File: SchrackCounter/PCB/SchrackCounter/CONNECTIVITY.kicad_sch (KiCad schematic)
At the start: 19 parts, among them J2 TYPE-C-31-M-12 (USB C CONN), U6 USBLC6-2SC6

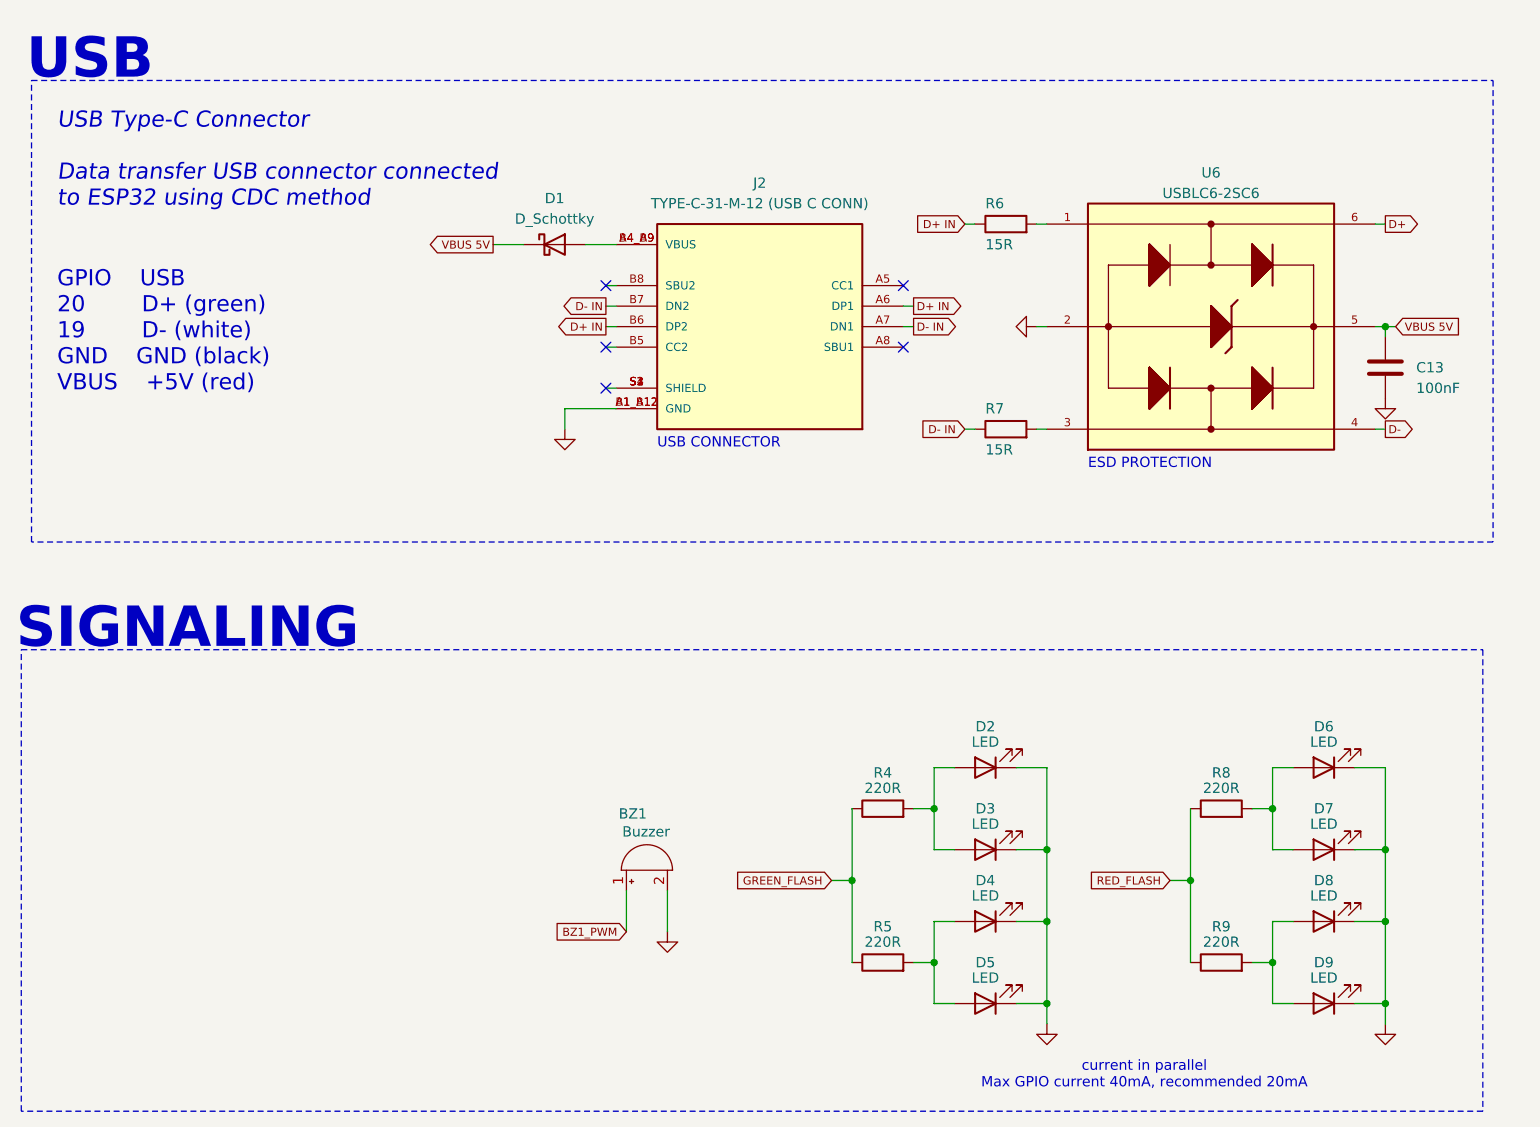
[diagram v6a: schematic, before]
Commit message: Schematic and PCB update
LDO Regulator, and some layout update
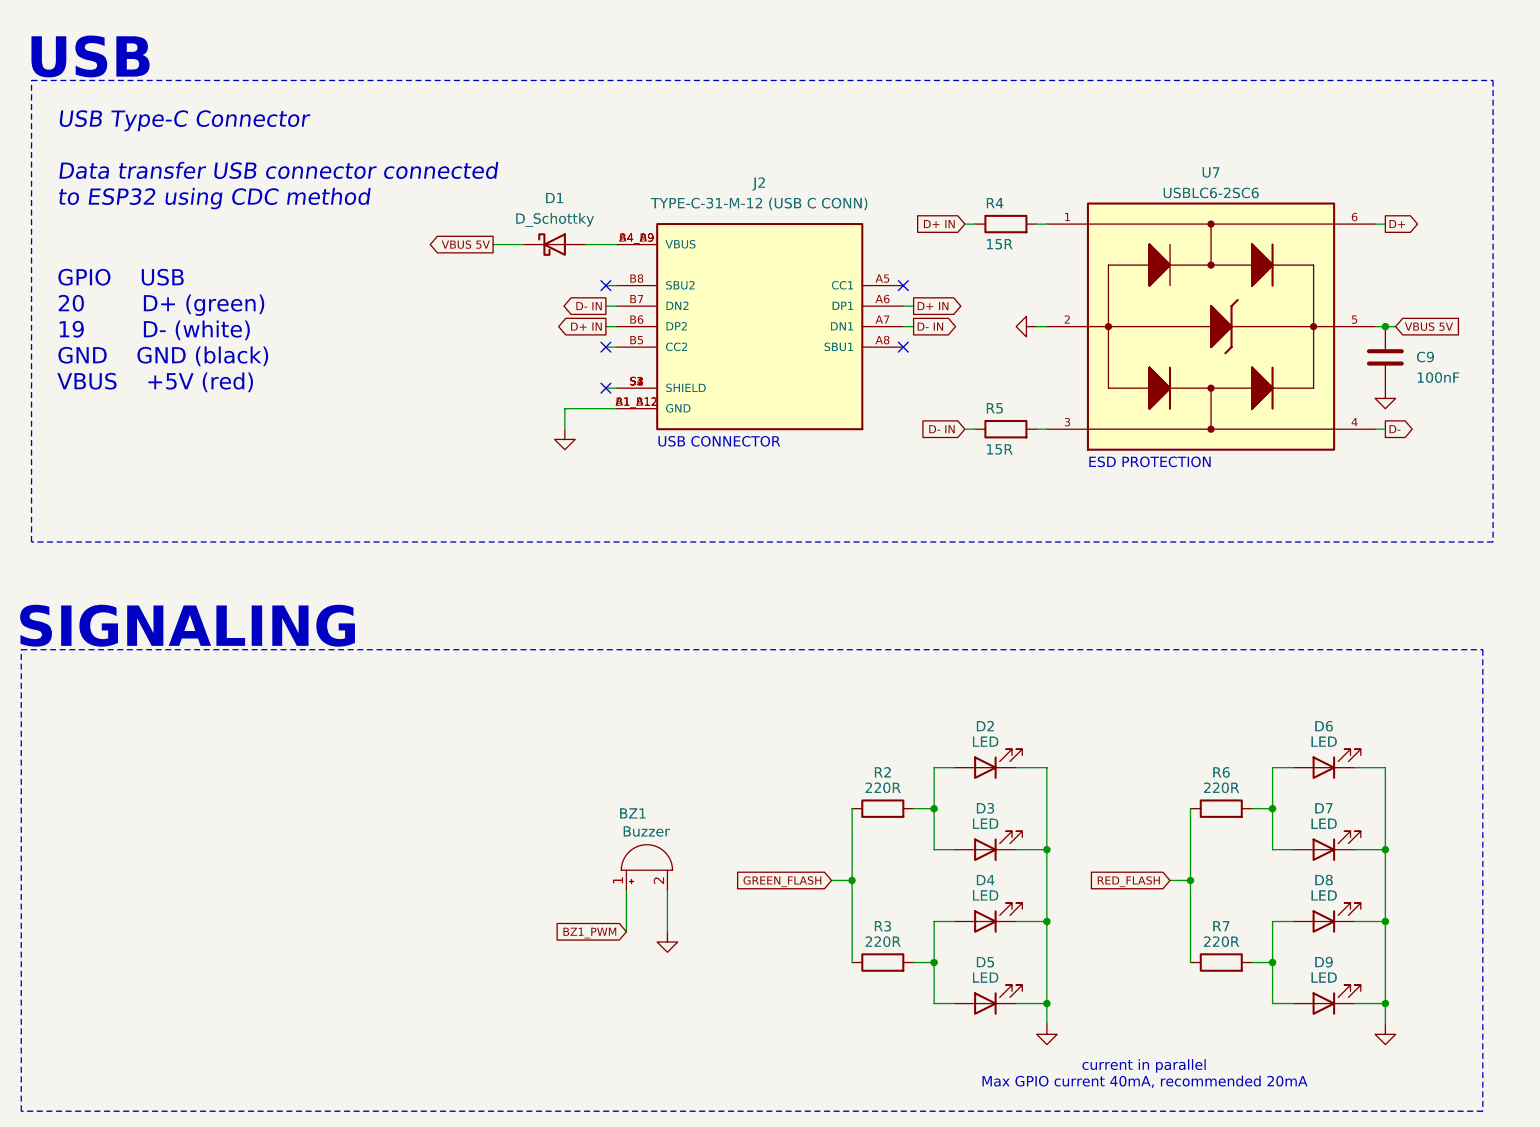
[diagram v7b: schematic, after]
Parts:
- renumbered C13 to C9, R4 to R2, R5 to R3, R6 to R4, R7 to R5, R8 to R6, R9 to R7, U6 to U7
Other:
- moved on the sheet: C9

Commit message: PCB Layout update
finished layout for the PCB will check for errors tommorow
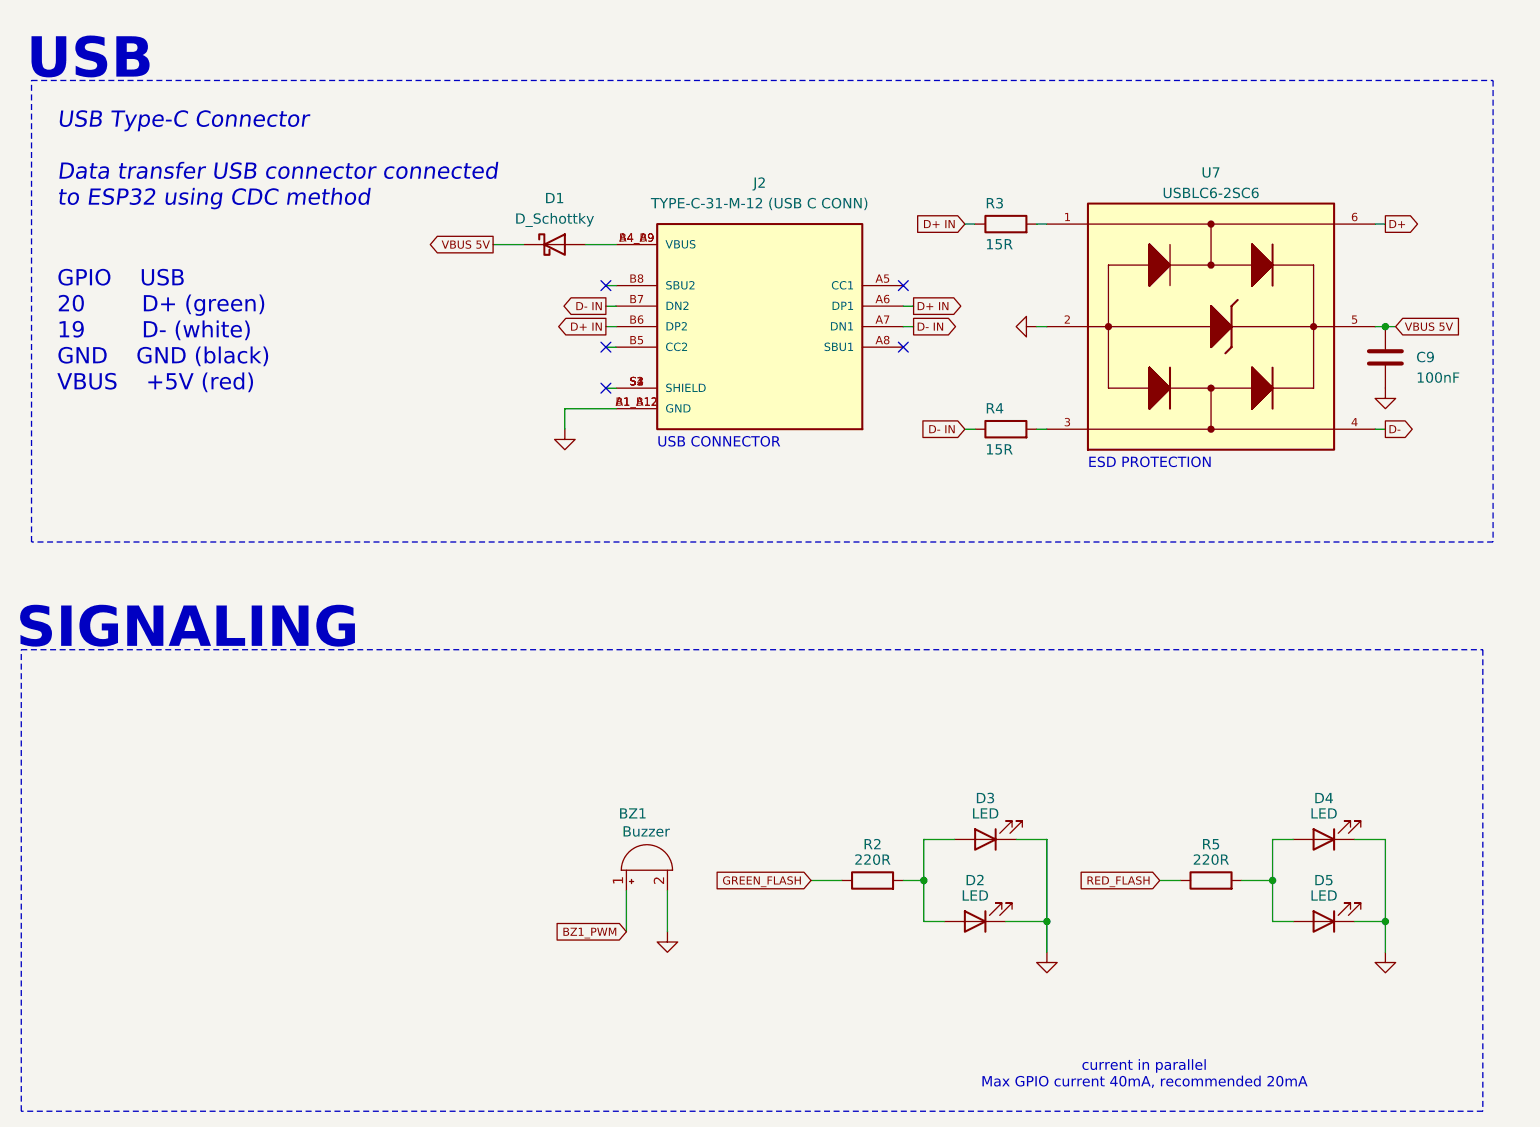
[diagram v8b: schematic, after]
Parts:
- removed D3, D5, D7, D9: LED, LED_SMD:LED_0805_2012Metric_Pad1.15x1.40mm_HandSolder, symbol Device:LED
- removed R2, R7: 220R, Resistor_SMD:R_0805_2012Metric_Pad1.20x1.40mm_HandSolder, symbol Device:R
- renumbered D4 to D2, D2 to D3, D6 to D4, D8 to D5, R3 to R2, R4 to R3, R5 to R4, R6 to R5
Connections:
- net at D2.2 (A), R2.2: now also D3.2 (A)
- net at D4.2 (A), R5.2: now also D5.2 (A)
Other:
- moved on the sheet: D2, D3, D4, R2, R5
